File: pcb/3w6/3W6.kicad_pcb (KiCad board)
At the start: 2 copper layers, 243.2 x 106 mm, 123 parts, among them J1 USB_C Main, J2 USB_C I2C_L, J3 USB_C I2C_R, SW1 SW_Push, SW10 SW_Push, SW11 SW_Push, SW12 SW_Push, SW13 SW_Push, SW14 SW_Push, SW15 SW_Push, SW16 SW_Push, SW17 SW_Push, SW18 SW_Push, SW19 SW_Push, SW2 SW_Push, SW20 SW_Push, SW21 SW_Push, SW22 SW_Push, SW23 SW_Push, SW24 SW_Push, SW25 SW_Push, SW26 SW_Push, SW27 SW_Push, SW28 SW_Push, SW29 SW_Push, SW3 SW_Push, SW30 SW_Push, SW31 SW_Push, SW32 SW_Push, SW33 SW_Push, SW34 SW_Push, SW35 SW_Push, SW36 SW_Push, SW37 SW_Push, SW4 SW_Push, SW5 SW_Push, SW6 SW_Push, SW7 SW_Push, SW8 SW_Push, SW9 SW_Push, U2 TCA9555RTWR, U3 ATmega32U4-MU, Y1 16MHZ

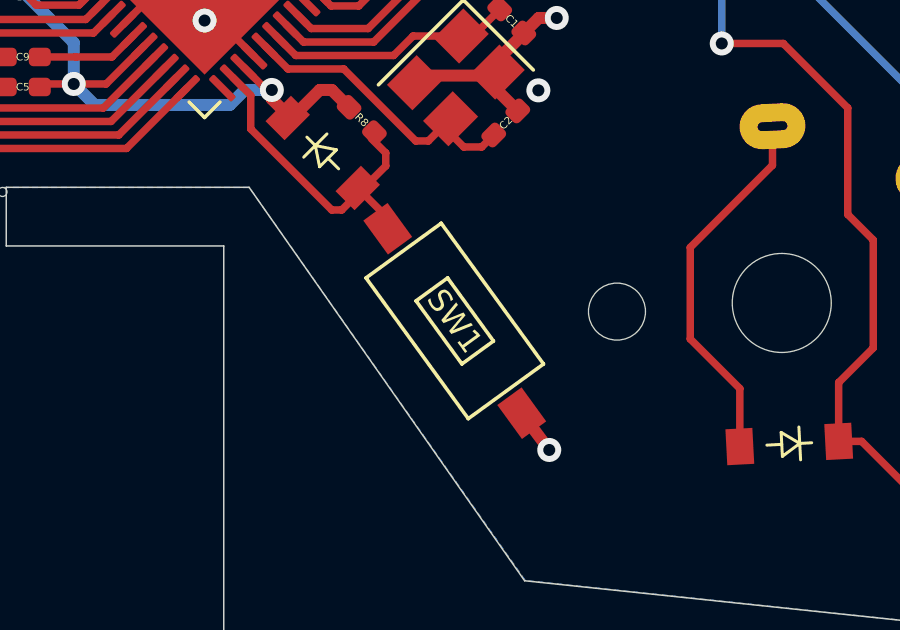
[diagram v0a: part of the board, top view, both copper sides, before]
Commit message: fix library paths to use included part library fix wrong value for crystal condensators
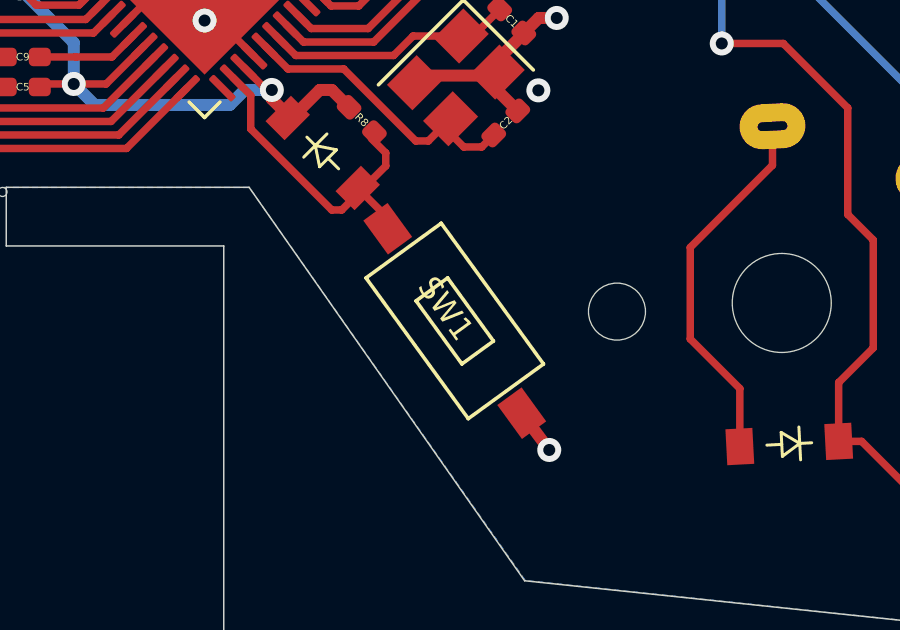
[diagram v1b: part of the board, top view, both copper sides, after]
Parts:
- C1, C2: value 22nF -> 22pF; footprint WetCorn:C_0402_HandSolder -> Weteor:C_0402_HandSolder
- C3, C4, C5, C6, C7, C8, C9: footprint WetCorn:C_0402_HandSolder -> Weteor:C_0402_HandSolder
- D1, D10, D11, D12, D13, D14, D15, D16, D17, D18, D19, D2, D20, D21, D22, D23, D24, D25, D26, D27, D28, D29, D3, D30, D31, D32, D33, D34, D35, D36, D37, D38, D39, D4, D40, D41, D42, D43, D44, D45, D46, D47, D48, D49, D5, D50, D51, D52, D53, D6, D7, D8, D9: footprint WetCorn:D_SOD-123 -> Weteor:D_SOD-123
- J1, J2, J3: footprint WetCorn:USB-C-12-Pin-MidMount -> Weteor:USB-C-12-Pin-MidMount
- R1, R2, R3, R4, R5, R6, R7, R8, R9: footprint WetCorn:R_0402_HandSolder -> Weteor:R_0402_HandSolder
- SW1: footprint WetCorn:Micro_Push_Button_3x6x2.5mm -> Weteor:Micro_Push_Button_3x6x2.5mm
- SW10, SW11, SW12, SW13, SW14, SW15, SW16, SW17, SW18, SW19, SW2, SW20, SW21, SW22, SW23, SW24, SW25, SW26, SW27, SW28, SW29, SW3, SW30, SW31, SW32, SW34, SW35, SW36, SW4, SW5, SW6, SW7, SW8, SW9: footprint WetCorn:Kailh_Choc_1u -> Weteor:Kailh_Choc_1u
- SW33, SW37: footprint WetCorn:Kailh_Choc_1.5u -> Weteor:Kailh_Choc_1.5u

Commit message: add: Pimoroni Trackball support
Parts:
- SW17: value SW_Push -> Trackball_Choc_Combi; footprint Weteor:Kailh_Choc_1u -> Weteor:trackball_choc_combi
- moved D17 20.3 mm to (211.0, 84.7), turned to 0 degrees
- moved C3 16.7 mm to (243.4, 83.4)
- moved R5 16.7 mm to (245.1, 84.0)
- moved U2 16.7 mm to (249.0, 83.5)
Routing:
- net /Col_R2: track 69.5 -> 114.7 mm, vias 0 -> 2
- net /Row_R3: track 71.4 -> 102.6 mm, vias 0 -> 2
- net /Col_R3: track 79.7 -> 102.8 mm, vias 1 -> 2
- net /Col_R4: track 99.7 -> 122.1 mm
- net /I2C_SDA_R: track 49.0 -> 68.2 mm
- net /I2C_SCL_R: track 48.0 -> 67.2 mm
- net VDD: track 57.7 -> 76.4 mm
- net /Row_R2: track 124.0 -> 107.3 mm
- net /Row_R1: track 143.4 -> 126.7 mm
- net /Row_R0: track 161.4 -> 144.7 mm
- net /Col_R0: track 74.5 -> 57.8 mm
- net /Col_R1: track 60.1 -> 43.8 mm
- net Net-(D17-Pad2): track 12.8 -> 27.3 mm
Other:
- outline, holes or cut-outs redrawn

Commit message: chg: uses atmega32u4-AU now
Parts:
- removed D1: D, Weteor:D_SOD-123
- removed U3: ATmega32U4-MU, Package_DFN_QFN:QFN-44-1EP_7x7mm_P0.5mm_EP5.2x5.2mm
- added U1: ATmega32U4-AU, Package_QFP:TQFP-44_10x10mm_P0.8mm, F.Cu at (89.7, 83.7)
- moved C5 20.7 mm to (95.1, 77.5), turned to 125 degrees
- moved C4 19.3 mm to (92.9, 91.8), turned to 125 degrees
- moved C2 16.8 mm to (76.4, 84.4), turned to 270 degrees
- moved R9 16.1 mm to (99.0, 86.0), turned to 215 degrees
- moved Y1 12.5 mm to (78.8, 84.5), turned to 90 degrees
- moved C1 11.9 mm to (81.2, 86.5), turned to 270 degrees
- moved C9 11.8 mm to (84.3, 77.0)
- moved C7 9.85 mm to (98.5, 82.3), turned to 215 degrees
- moved R8 5.87 mm to (92.0, 92.4), turned to 305 degrees
- moved C8 4.82 mm to (82.6, 77.5), turned to 270 degrees
- moved C6 2.21 mm to (80.8, 77.5), turned to 270 degrees
- moved SW1 1.25 mm to (91.7, 95.9), turned to 125 degrees
- moved D42 0.51 mm to (128.0, 66.2)
- moved D40 0.50 mm to (128.0, 49.3)
- moved D38 0.40 mm to (46.6, 55.8)
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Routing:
- net GND: track 46.5 -> 30.2 mm, vias 17 -> 18
- net /Row_L3: track 86.6 -> 71.0 mm, vias 2 -> 0
- net /Col_L1: track 54.9 -> 70.0 mm
- net /Col_L3: track 92.3 -> 105.5 mm, vias 0 -> 1
- net /D-: track 55.4 -> 65.8 mm
- net /D+: track 56.6 -> 66.0 mm
- net Net-(R8-Pad2): track 10.9 -> 19.0 mm, vias 0 -> 2
- net +5V: track 176.1 -> 170.3 mm, vias 10 -> 6
- net Net-(U3-Pad38): track 3.07 -> 0.00 mm, vias 1 -> 0
- net Net-(U3-Pad41): track 2.70 -> 0.00 mm, vias 1 -> 0
- net /Row_L0: track 154.3 -> 156.9 mm
- net Net-(U3-Pad21): track 2.40 -> 0.00 mm, vias 1 -> 0
- net Net-(U3-Pad37): track 2.20 -> 0.00 mm, vias 1 -> 0
- net /Row_L1: track 136.9 -> 138.4 mm
- net Net-(U3-Pad42): track 1.54 -> 0.00 mm, vias 1 -> 0
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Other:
- outline, holes or cut-outs redrawn
